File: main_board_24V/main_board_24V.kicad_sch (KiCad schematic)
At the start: 18 parts, among them J1 WJ126V-5.0-06P-14-00A, U2 TLV75733PDBV

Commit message: continued schematic design
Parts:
- removed R?: 13k3, Resistor_SMD:R_0402_1005Metric, symbol Device:R_Small
- added Q3: MMBT5551, Package_TO_SOT_SMD:SOT-23, symbol Device:Q_NPN_BEC
- added R11, R12: 100k, Resistor_SMD:R_0402_1005Metric, symbol Device:R_Small
- added U1: MCU Board, sonoff:pcb_mcu, symbol sonoff:mcu
- added U3: MCU Relais, sonoff:pcb_relais, symbol sonoff:relais
- L?: footprint Inductor_SMD:L_Chilisin_BMRx00060630 -> Inductor_SMD:L_Sunlord_SWPA4030S; LCSC Part # C439009 -> C15269; Rating 6.5A 24mR -> 2.4A 52mR
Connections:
- net +24V: now also U3.4 (V_{in}), U3.5 (V_{in})
- net +3V3: now also R12.2, U1.3 (VCC)
- net +5V: now also U3.1 (VCC)
- net GND: now also U?.13 (RT), Q3.2 (E), U1.1 (GND), U1.2 (GND), U3.3 (GND)
- net V_{out}: now reaches J1.3 (Pin_3)
- net V_{out}: now also U3.6 (V_{out})
- net at J1.6 (Pin_6): now also R11.2
- new net: Q3.3 (C), R12.1, U1.4 (~{in})
- new net: U1.5 (out), U3.2 (in)
- new net: Q3.1 (B), R11.1
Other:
- note added: "set to 2.2MHz"
- note added: "way too powerful IC, used here for convenience"
- note removed: "can be set to 2.2MHz"
- note removed: "set to 1.2MHz"
- note removed: "yes, it is vastly oversized"
- moved on the sheet: J1

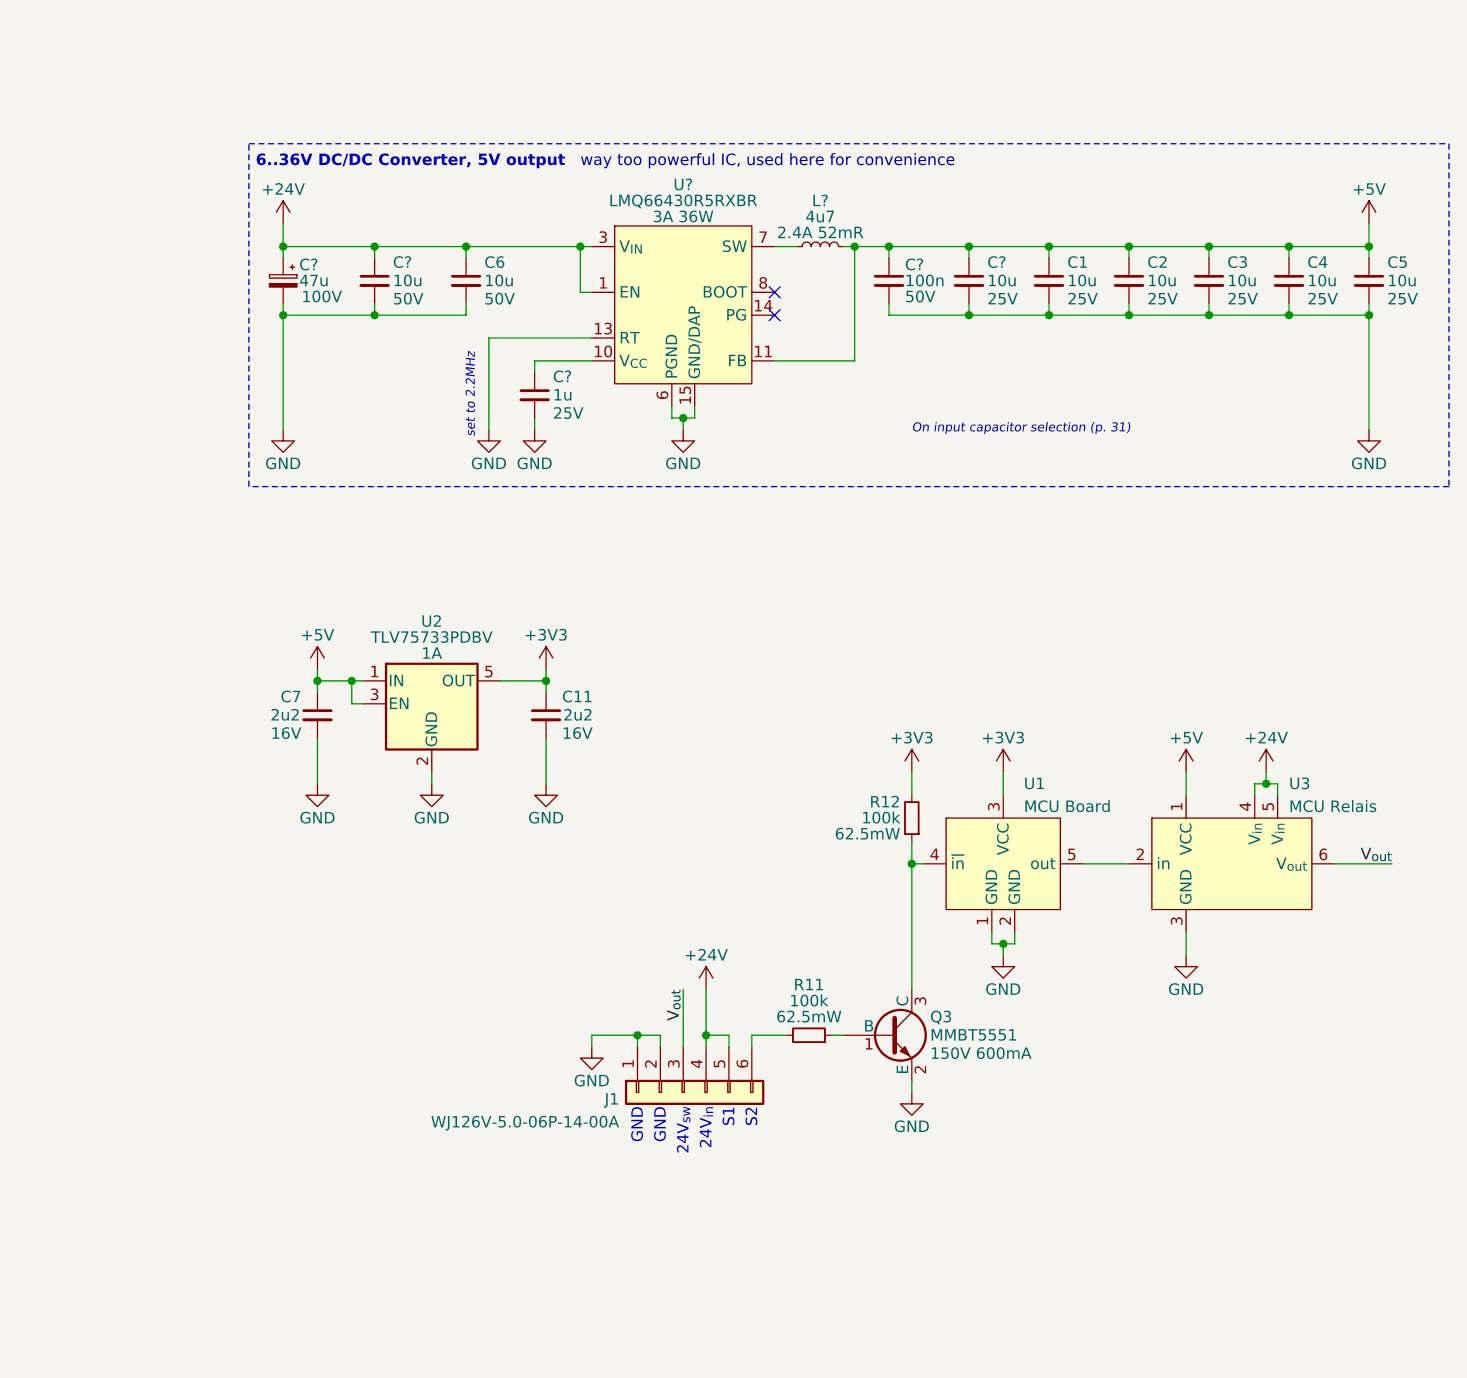
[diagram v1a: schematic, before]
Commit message: routed PCB
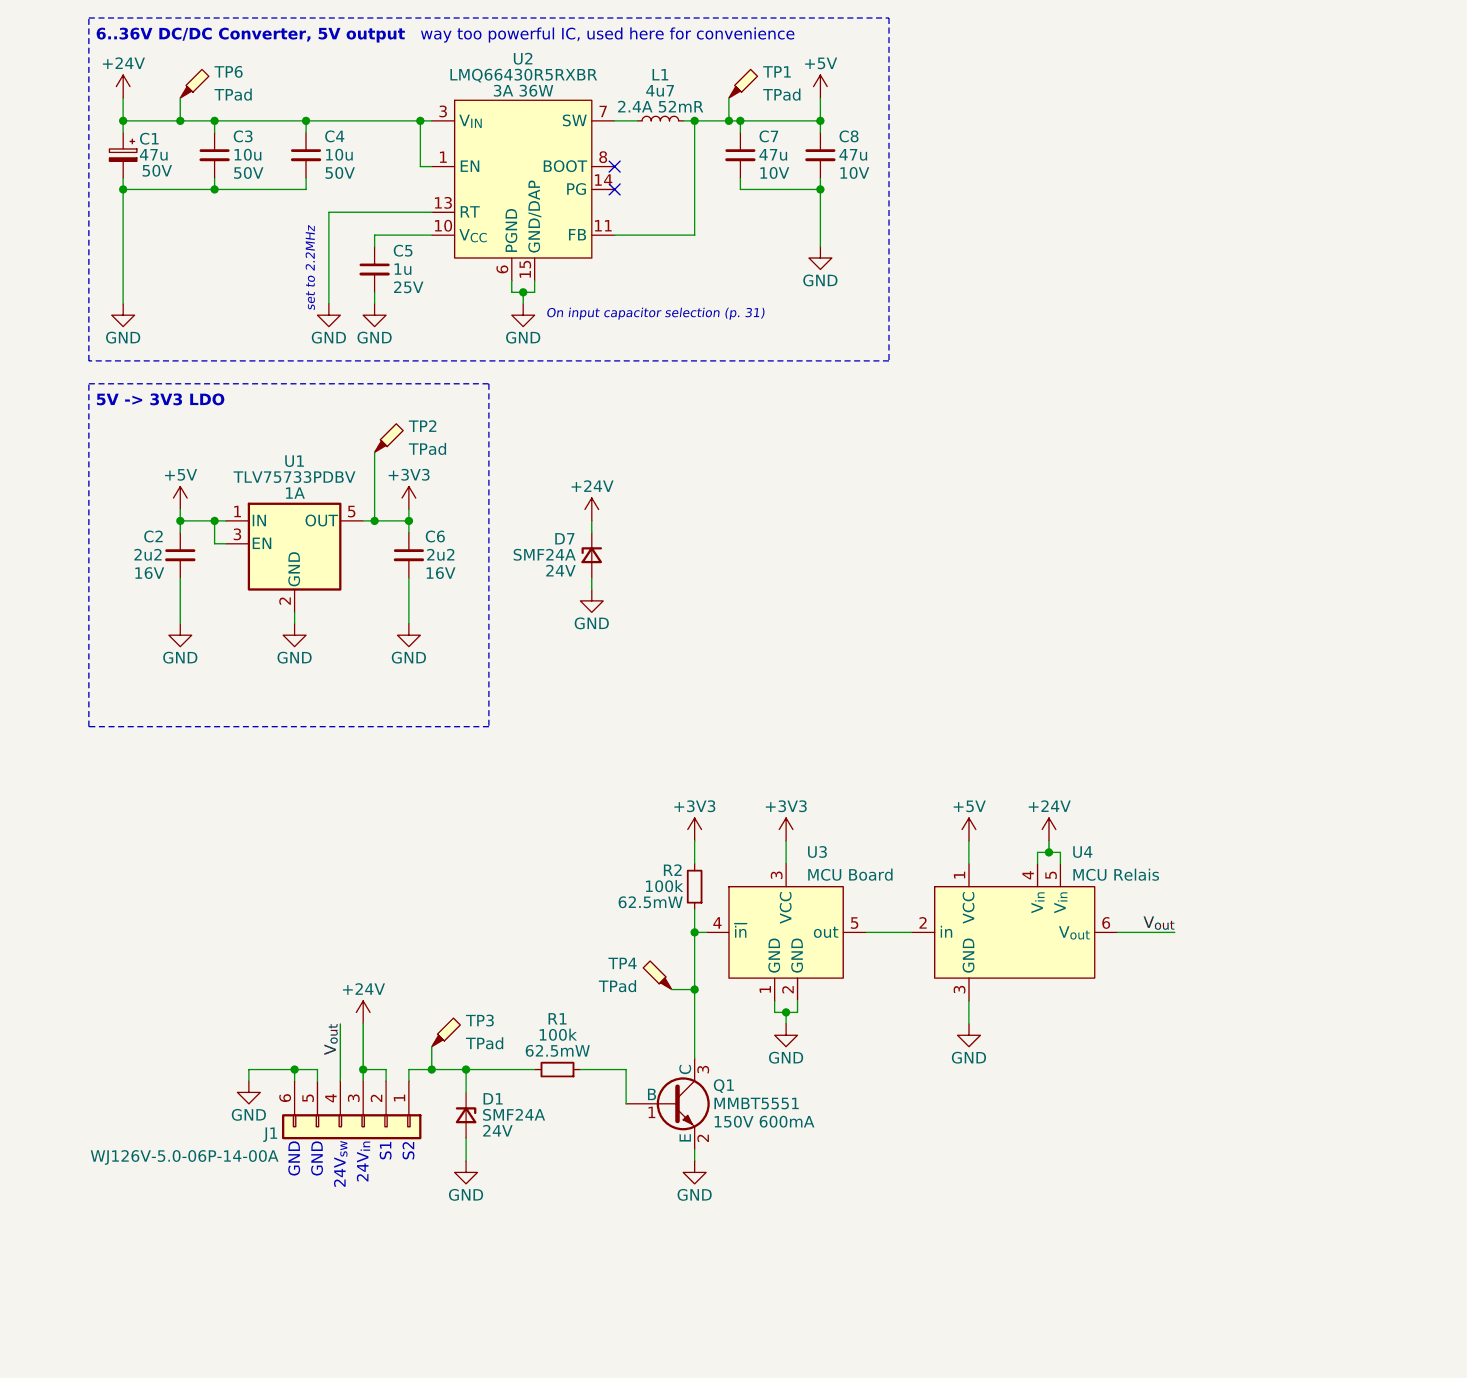
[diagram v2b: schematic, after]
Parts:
- removed C1, C2, C3, C4, C?: 10u, Capacitor_SMD:C_0805_2012Metric, symbol Device:C_Small
- removed C?: 100n, Capacitor_SMD:C_0402_1005Metric, symbol Device:C_Small
- removed U?: LMQ66430R5RXBR, #LibroDuctLib:TI_VQFN_15_EP, symbol #LibroDuctLib:LMQ664x0
- added C7: 47u, Capacitor_SMD:C_1206_3216Metric, symbol Device:C_Small
- added D1, D7: SMF24A, Diode_SMD:D_SOD-123F, symbol Device:D_Zener_Small
- added TP1, TP2, TP3, TP4, TP6: TPad, TestPoint:TestPoint_Pad_D1.0mm, symbol Connector:TestPoint_Probe
- added U2: LMQ66430R5RXBR, #TimGollLib:TI_VQFN_15_EP, symbol #TimGollLib:LMQ66430R5RXBR
- C1: renamed from C?; footprint Capacitor_SMD:CP_Elec_8x10.5 -> Capacitor_SMD:CP_Elec_6.3x7.7; LCSC Part # C18203173 -> C3349; Rating 100V -> 50V
- C8: renamed from C5; value 10u -> 47u; footprint Capacitor_SMD:C_0805_2012Metric -> Capacitor_SMD:C_1206_3216Metric; LCSC Part # C45783 -> C96123; Rating 25V -> 10V
- gave numbers to parts that had none: 3
- renumbered C7 to C2, C6 to C4, C11 to C6, Q3 to Q1, R11 to R1, R12 to R2, U2 to U1, U1 to U3, U3 to U4
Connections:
- net +24V: now also J1.2 (Pin_2), J1.3 (Pin_3), D7.1 (K), TP6.1, U2.1 (EN), U2.3 (V_{IN}); no longer J1.4 (Pin_4), J1.5 (Pin_5)
- net +3V3: now also TP2.1
- net +5V: now also C7.1, TP1.1, U2.11 (FB)
- net GND: now also J1.5 (Pin_5), J1.6 (Pin_6), C7.2, D1.2 (A), D7.2 (A), U2.13 (RT), U2.15 (GND/DAP), U2.6 (PGND); no longer J1.1 (Pin_1), J1.2 (Pin_2)
- net V_{out}: now also J1.4 (Pin_4); no longer J1.3 (Pin_3)
- net at C5.1: now also U2.10 (V_{CC})
- net at Q1.3 (C), R2.1, U3.4 (~{in}): now also TP4.1
- net at L1.1: now also U2.7 (SW)
- net at R1.2: now also J1.1 (Pin_1), D1.1 (K), TP3.1; no longer J1.6 (Pin_6)
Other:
- note added: "5V -> 3V3 LDO"
- moved on the sheet: C1, C2, C3, C4, C5, C6, C8, J1, L1, Q1, R1, R2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

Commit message: small fixes; production files
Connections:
- net +3V3: now also U3.5 (VCC); no longer U3.3 (VCC)
- net at U4.2 (in): now also U3.3 (out); no longer U3.5 (out)
